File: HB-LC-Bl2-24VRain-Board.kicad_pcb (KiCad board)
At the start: 2 copper layers, 100 x 100 mm, 36 parts, among them IC1 ArduinoProMini, J2 Taster Markise1, J3 Taster Markise 2, J4 Regensensor, J5 230V, J6 Motor1, J7 Motor2, Q1 BC337, Q2 BC337, Q3 BC337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

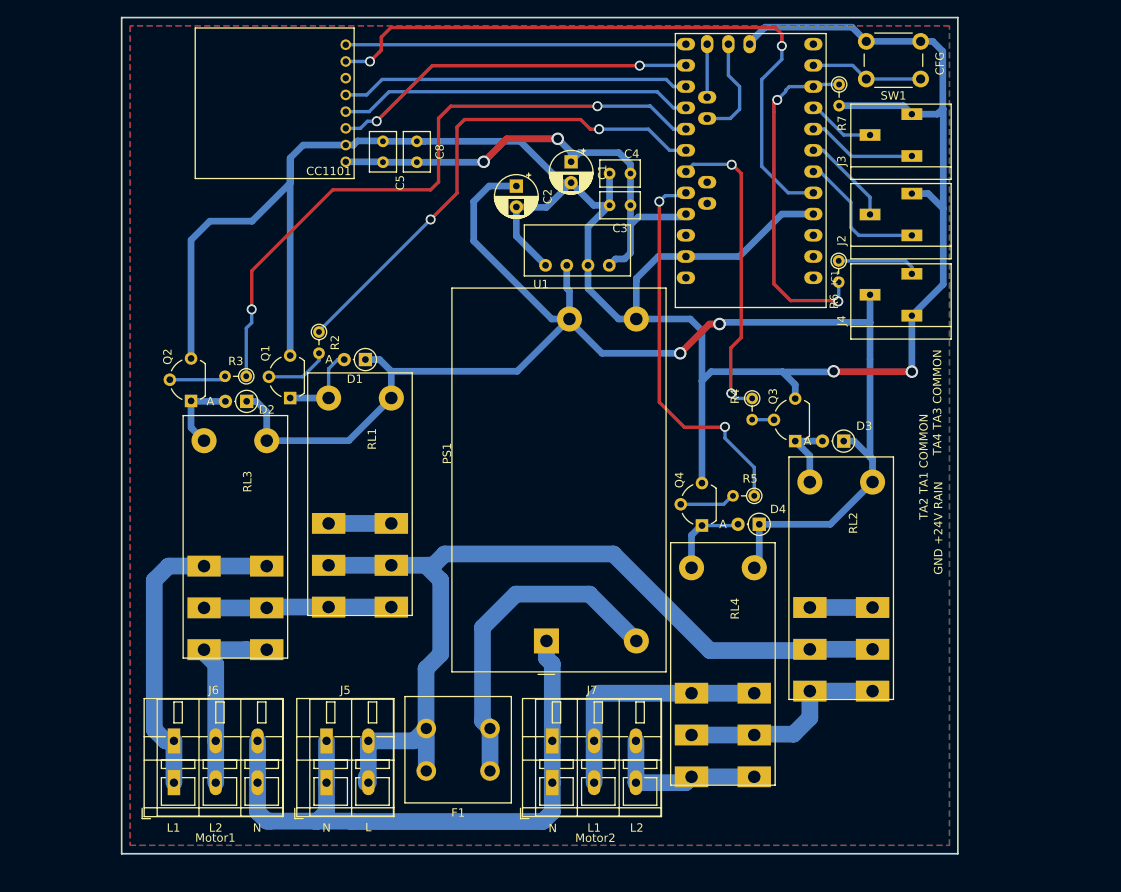
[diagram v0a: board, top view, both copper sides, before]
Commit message: Several schematic updates
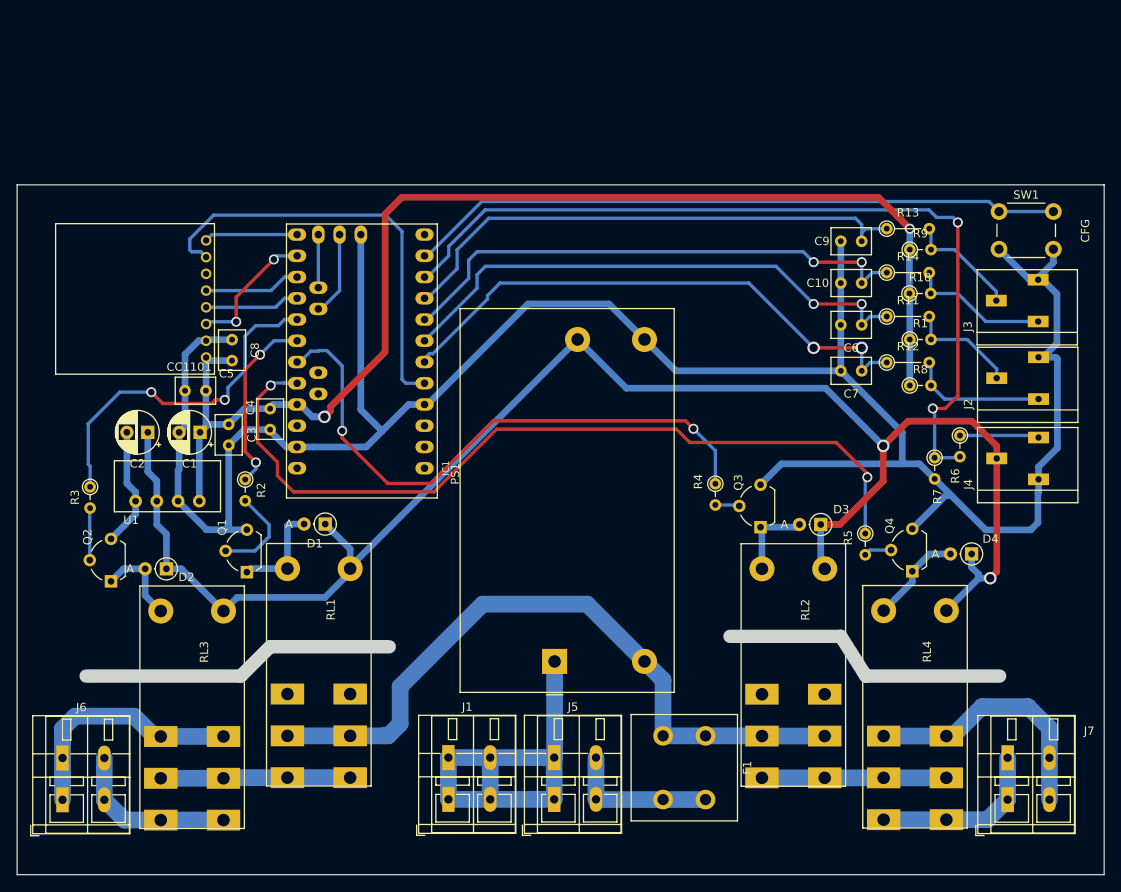
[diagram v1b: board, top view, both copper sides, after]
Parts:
- added C10: 100n, Capacitor_THT:C_Rect_L4.6mm_W3.0mm_P2.50mm_MKS02_FKP02, F.Cu at (113.5, 56.8)
- added C6: 100n, Capacitor_THT:C_Rect_L4.6mm_W3.0mm_P2.50mm_MKS02_FKP02, F.Cu at (113.5, 61.8)
- added C7: 100n, Capacitor_THT:C_Rect_L4.6mm_W3.0mm_P2.50mm_MKS02_FKP02, F.Cu at (113.5, 67.2)
- added C9: 100n, Capacitor_THT:C_Rect_L4.6mm_W3.0mm_P2.50mm_MKS02_FKP02, F.Cu at (113.5, 51.8)
- added J1: Motor_N, TerminalBlock_WAGO:TerminalBlock_WAGO_236-102_1x02_P5.00mm_45Degree, F.Cu at (64.1, 118.5)
- added R1: 10k, Resistor_THT:R_Axial_DIN0204_L3.6mm_D1.6mm_P2.54mm_Vertical, F.Cu at (119.2, 63.5)
- added R10: 10k, Resistor_THT:R_Axial_DIN0204_L3.6mm_D1.6mm_P2.54mm_Vertical, F.Cu at (119.2, 58.0)
- added R11: 47, Resistor_THT:R_Axial_DIN0204_L3.6mm_D1.6mm_P5.08mm_Vertical, F.Cu at (116.5, 60.8)
- added R12: 47, Resistor_THT:R_Axial_DIN0204_L3.6mm_D1.6mm_P5.08mm_Vertical, F.Cu at (116.5, 66.2)
- added R13: 47, Resistor_THT:R_Axial_DIN0204_L3.6mm_D1.6mm_P5.08mm_Vertical, F.Cu at (116.5, 50.2)
- added R14: 47, Resistor_THT:R_Axial_DIN0204_L3.6mm_D1.6mm_P5.08mm_Vertical, F.Cu at (116.5, 55.5)
- added R8: 10k, Resistor_THT:R_Axial_DIN0204_L3.6mm_D1.6mm_P2.54mm_Vertical, F.Cu at (119.2, 69.0)
- added R9: 10k, Resistor_THT:R_Axial_DIN0204_L3.6mm_D1.6mm_P2.54mm_Vertical, F.Cu at (119.2, 52.8)
- J6, J7: footprint TerminalBlock_WAGO:TerminalBlock_WAGO_236-103_1x03_P5.00mm_45Degree -> TerminalBlock_WAGO:TerminalBlock_WAGO_236-102_1x02_P5.00mm_45Degree
- R6: value 68k -> 6k8
- R7: value 10k -> 1k
- moved U1 56.6 mm to (24.1, 84.1)
- moved C1 54.9 mm to (34.4, 74.6), turned to 180 degrees
- moved C3 54.7 mm to (37.8, 73.7), turned to 270 degrees
- moved J7 54.5 mm to (130.9, 118.5)
- moved C2 53.0 mm to (28.1, 74.6), turned to 180 degrees
- moved IC1 51.8 mm to (53.6, 64.9)
- moved C4 51.5 mm to (42.8, 71.8), turned to 270 degrees
- moved R7 46.1 mm to (122.2, 77.6)
- moved C5 38.1 mm to (32.6, 69.6), turned to 0 degrees
- moved C8 32.4 mm to (38.2, 63.5)
- moved U3 28.7 mm to (35.1, 58.6)
- moved J5 27.3 mm to (76.7, 118.5)
- moved F1 26.1 mm to (94.8, 110.9), turned to 270 degrees
- moved Q4 25.7 mm to (119.5, 91.2)
- moved D4 25.6 mm to (126.7, 89.2)
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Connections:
- J2 pad 1: /TA2 -> /TA2_IN
- J2 pad 2: /TA1 -> /TA1_IN
- J3 pad 1: /TA4 -> /TA4_IN
- J3 pad 2: /TA3 -> /TA3_IN
- J7 pad 1: /N -> /M2_L2
- RL1 pad 11: /L -> /L_FUSED
- RL1 pad 21: /L -> /L_FUSED
- RL2 pad 11: /L -> /L_FUSED
- RL2 pad 21: /L -> /L_FUSED
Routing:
- net /L: track 110.8 -> 18.1 mm
- net +3V3: track 59.1 -> 149.0 mm
- net Net-(IC1-Pad11): track 13.5 -> 78.4 mm
- net /RAIN: track 41.3 -> 101.8 mm
- net /TA3: track 8.13 -> 63.1 mm
- net /TA1: track 11.2 -> 64.7 mm, vias 0 -> 2
- net /M2_DIR: track 46.4 -> 99.7 mm
- net /TA4: track 13.2 -> 63.5 mm, vias 0 -> 2
- net /TA2: track 16.7 -> 66.1 mm, vias 0 -> 2
- net /L_FUSED: track 39.9 -> 83.8 mm
- net /M1_EN: track 60.6 -> 21.8 mm
- net /M1_DIR: track 78.6 -> 42.0 mm
- net /M2_EN: track 37.0 -> 70.8 mm
- net /RF_SCLK: track 42.5 -> 11.3 mm
- net /RF_MISO: track 41.8 -> 11.5 mm
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- removed copper zone on B.Cu, net GND
- removed copper zone on F.Cu, net GND
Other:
- board size 100 x 100 mm -> 130 x 82.5 mm
- net class 230V: clearance 2.5 -> 3
- board text added: "M1 L1"
- board text added: "M1 N"
- board text added: "M1_L2"
- board text added: "M2 L1"
- board text added: "M2 L2"
- board text added: "M2 N"
- board text added: "T2 T1 GND"
- board text added: "T4 T3 GND"
- board text removed: "L1"
- board text removed: "L2"
- board text removed: "Motor1"
- board text removed: "Motor2"
- board text removed: "TA2 TA1 COMMON"
- board text removed: "TA4 TA3 COMMON"

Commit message: Few updates to layout. But not yet done.
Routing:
- added copper zone on B.Cu, net GND
- added copper zone on F.Cu, net GND
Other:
- board text added: "M1 L2"
- board text removed: "M1_L2"

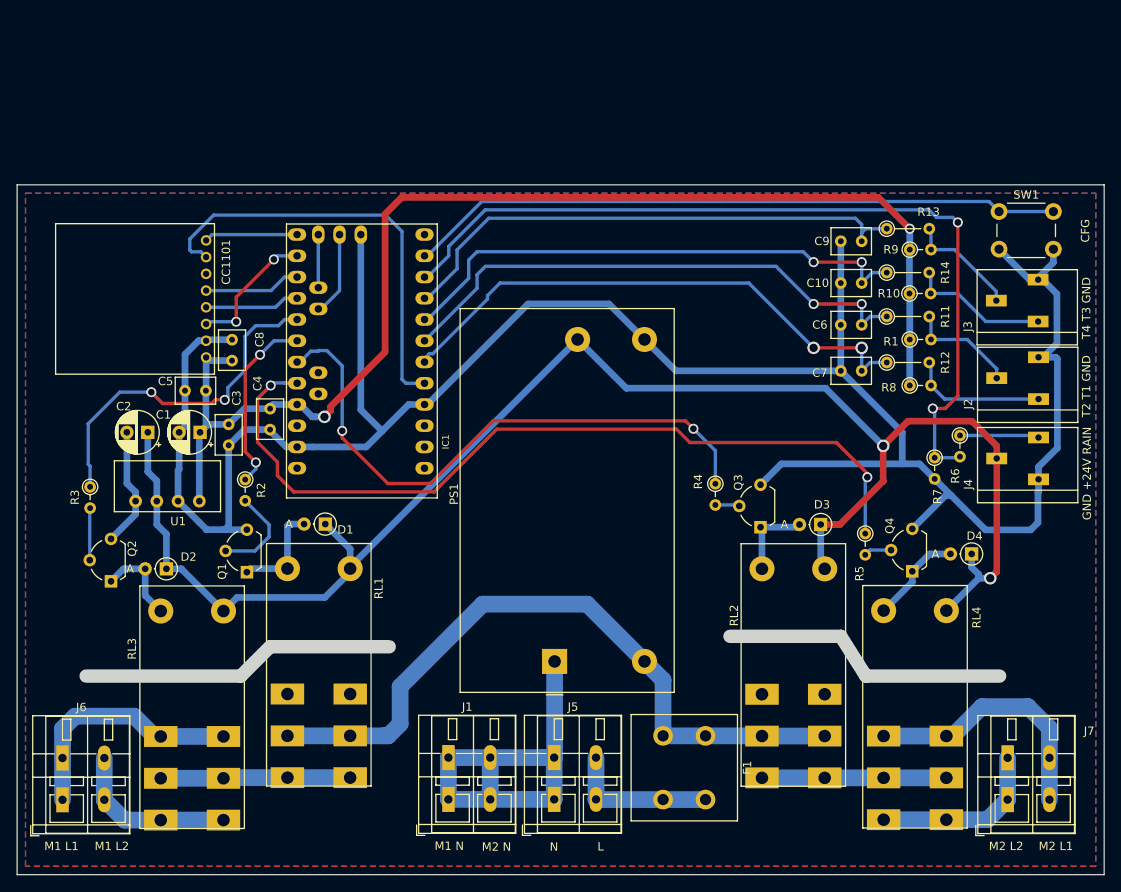
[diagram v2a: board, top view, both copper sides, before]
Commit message: Version 1.0
- Some beautifications done
- Replaced 2x100nF at CC1101 at Arduino woth 1uF each
- Fixed the base resistor for the relay control
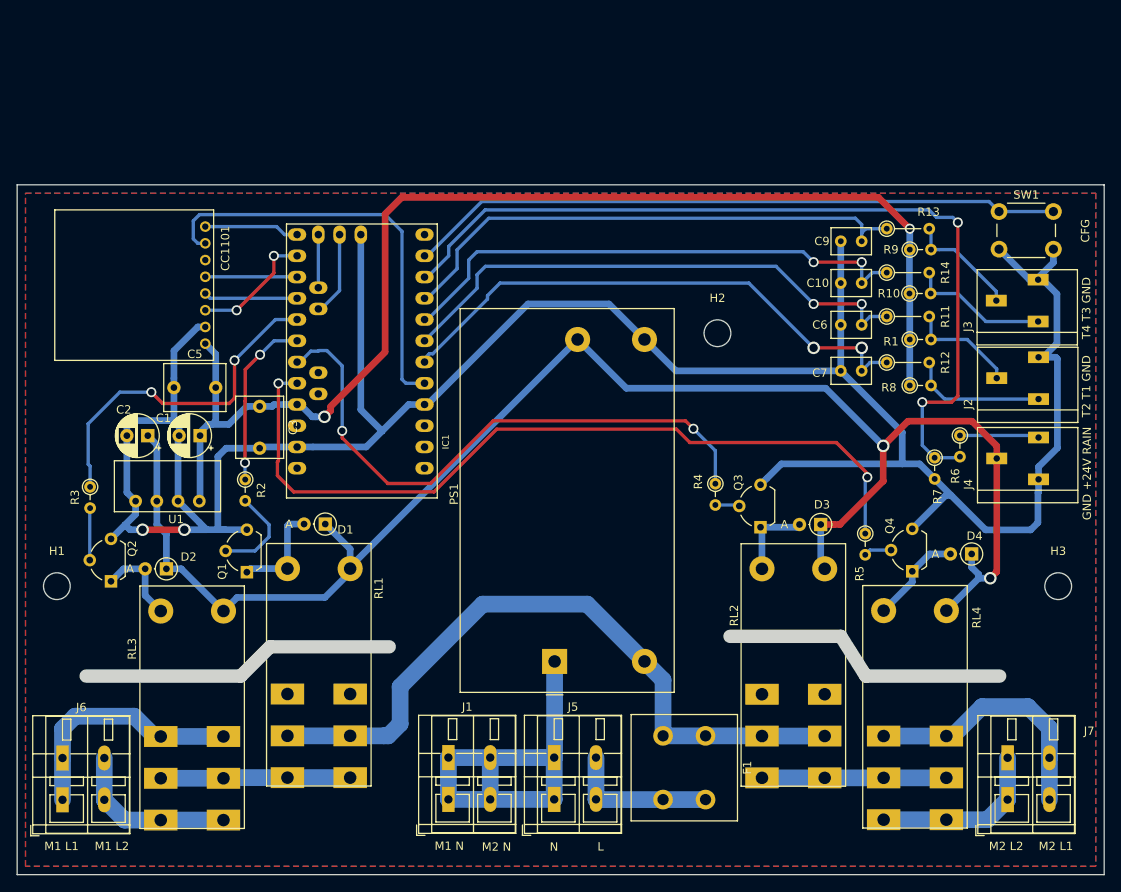
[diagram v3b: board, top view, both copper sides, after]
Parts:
- removed C4, C8: 100n, Capacitor_THT:C_Rect_L4.6mm_W3.0mm_P2.50mm_MKS02_FKP02
- added H1: MountingHole, MountingHole:MountingHole_3.2mm_M3, F.Cu at (17.2, 93.0)
- added H2: MountingHole, MountingHole:MountingHole_3.2mm_M3, F.Cu at (96.2, 62.8)
- added H3: MountingHole, MountingHole:MountingHole_3.2mm_M3, F.Cu at (137.0, 93.0)
- C3, C5: value 100n -> 1u; footprint Capacitor_THT:C_Rect_L4.6mm_W3.0mm_P2.50mm_MKS02_FKP02 -> Capacitor_THT:C_Rect_L7.2mm_W5.5mm_P5.00mm_FKS2_FKP2_MKS2_MKP2
- R2, R3, R4, R5: value 10k -> 2k4
- moved C3 4.28 mm to (41.5, 71.5)
- moved U3 1.65 mm to (35.0, 57.0)
- moved C5 1.38 mm to (31.2, 69.2)
- moved C1 0.40 mm to (34.4, 75.0)
- moved C2 0.40 mm to (28.1, 75.0)
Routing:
- net GND: track 287.4 -> 302.4 mm, vias 0 -> 2
- net /M2_DIR: track 99.7 -> 97.3 mm
- net /RAIN: track 101.8 -> 104.0 mm
- net +3V3: track 149.0 -> 146.8 mm
- net /RF_MOSI: track 16.0 -> 14.9 mm
- net /RF_INT: track 51.6 -> 50.5 mm
- net /M1_EN: track 21.8 -> 20.8 mm
- net /RF_MISO: track 11.5 -> 11.0 mm
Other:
- net class 230V: clearance 3 -> 2.5
- rule via_min_size: 0 -> 0.8

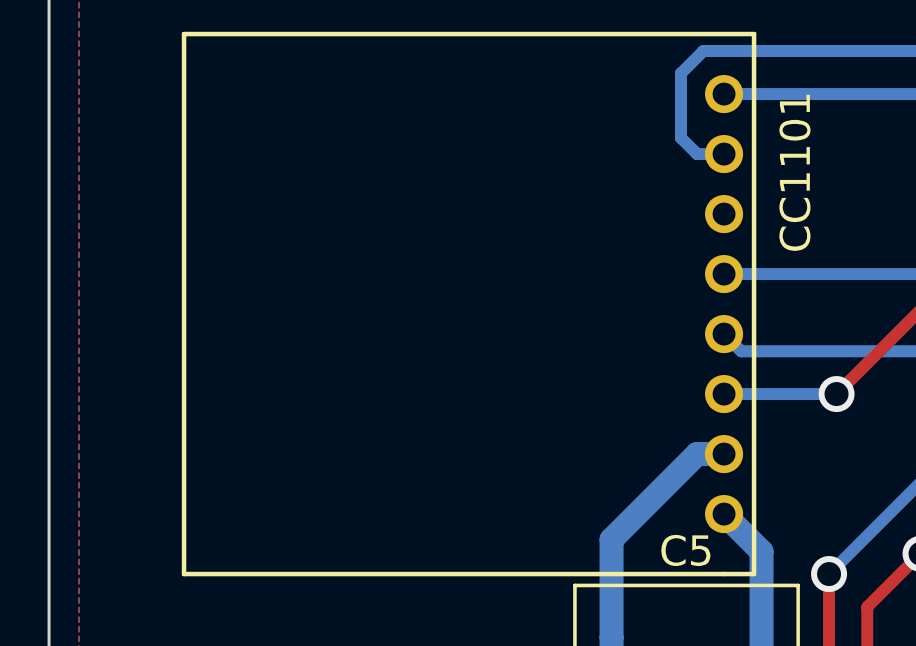
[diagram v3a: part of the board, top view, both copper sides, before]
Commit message: Added missing GND connections of CC101
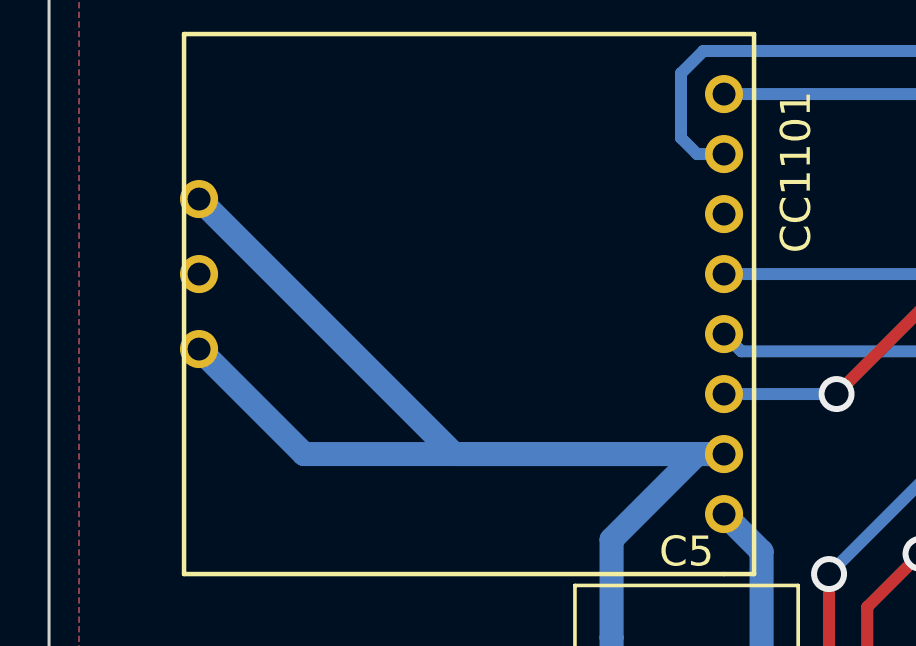
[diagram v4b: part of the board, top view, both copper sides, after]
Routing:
- net GND: track 302.4 -> 342.3 mm
